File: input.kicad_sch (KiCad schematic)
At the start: 32 parts, among them J15 Screw_Terminal_01x02, J6 Screw_Terminal_01x04, J7 Screw_Terminal_01x04, U2 ADS1113IDGS, U3 TCA9517ADGK, U5 LTV-847S, U6 LTV-847S

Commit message: added part numbers
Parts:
- C1, C2, C3: LCSC (none) -> C49678
- D1, D2, D3, D4, D5, D6, D7, D8: footprint LED_SMD:LED_1206_3216Metric -> LED_SMD:LED_0805_2012Metric_Pad1.15x1.40mm_HandSolder; LCSC (none) -> C2297
- J15: footprint (none) -> Connector_Phoenix_MC:PhoenixContact_MC_1,5_2-G-3.5_1x02_P3.50mm_Horizontal; LCSC (none) -> C61791
- J6, J7: footprint (none) -> Connector_Phoenix_MC:PhoenixContact_MC_1,5_4-G-3.5_1x04_P3.50mm_Horizontal; LCSC (none) -> C5241865
- R1, R2, R3, R4, R5, R6, R7, R8: LCSC (none) -> C17513
- R10, R9: LCSC (none) -> C17477
- U2: LCSC (none) -> C2651336
- U3: LCSC (none) -> C544515
- U5: LCSC (none) -> C114599

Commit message: larger pcb
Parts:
- JP1, JP2: footprint (none) -> Jumper:SolderJumper-2_P1.3mm_Open_Pad1.0x1.5mm
- TP12, TP13: footprint (none) -> TestPoint:TestPoint_Pad_D1.5mm
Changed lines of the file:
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@@
 			)
 		)
-		(property "Footprint" ""
+		(property "Footprint" "Jumper:SolderJumper-2_P1.3mm_Open_Pad1.0x1.5mm"
 			(at 201.93 92.71 0)
 			(effects
@@
 		)
 		(property "Description" "Solder Jumper, 2-pole, open"
+			(at 201.93 92.71 0)
+			(effects
+				(font
+					(size 1.27 1.27)
+				)
+				(hide yes)
+			)
+		)
+		(property "LCSC" ""
 			(at 201.93 92.71 0)
 			(effects
@@
 			)
 		)
-		(property "Footprint" ""
+		(property "Footprint" "TestPoint:TestPoint_Pad_D1.5mm"
 			(at 217.17 59.69 0)
 			(effects
@@
 		)
 		(property "Description" "test point"
+			(at 212.09 59.69 0)
+			(effects
+				(font
+					(size 1.27 1.27)
+				)
+				(hide yes)
+			)
+		)
+		(property "LCSC" ""
 			(at 212.09 59.69 0)
 			(effects
@@
 			)
 		)
-		(property "Footprint" ""
+		(property "Footprint" "TestPoint:TestPoint_Pad_D1.5mm"
 			(at 227.33 59.69 0)
 			(effects
@@
 		)
 		(property "Description" "test point"
+			(at 222.25 59.69 0)
+			(effects
+				(font
+					(size 1.27 1.27)
+				)
+				(hide yes)
+			)
+		)
+		(property "LCSC" ""
 			(at 222.25 59.69 0)
 			(effects
@@
 			)
 		)
-		(property "Footprint" ""
+		(property "Footprint" "Jumper:SolderJumper-2_P1.3mm_Open_Pad1.0x1.5mm"
 			(at 201.93 102.87 0)
 			(effects
@@
 			(at 201.93 102.87 0)
 			(effects
+				(font
+					(size 1.27 1.27)
+				)
+				(hide yes)
+			)
+		)
+		(property "LCSC" ""
+			(at 201.93 102.87 0)
+			(effects

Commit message: added fuse and c for 7805
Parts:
- removed C1, C2: 100nF, Capacitor_SMD:C_0805_2012Metric_Pad1.18x1.45mm_HandSolder, symbol Device:C
- removed U3: TCA9517ADGK, Package_SO:VSSOP-8_3x3mm_P0.65mm, symbol Logic_LevelTranslator:TCA9517ADGK
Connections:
- net SCL: now also JP2.2 (B), TP13.1, U2.10 (SCL)
- net SDA: now also JP1.2 (B), TP12.1, U2.9 (SDA)
- net +5V renamed VCC
- no-connect marks 1 -> 0

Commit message: hat routing finished
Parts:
- R1, R2, R3, R4, R5, R6, R7, R8: footprint Resistor_SMD:R_0805_2012Metric -> Resistor_SMD:R_0805_2012Metric_Pad1.20x1.40mm_HandSolder
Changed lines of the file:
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@@
 			)
 		)
-		(property "Footprint" "Resistor_SMD:R_0805_2012Metric"
+		(property "Footprint" "Resistor_SMD:R_0805_2012Metric_Pad1.20x1.40mm_HandSolder"
 			(at 72.39 32.258 90)
 			(effects
@@
 			)
 		)
-		(property "Footprint" "Resistor_SMD:R_0805_2012Metric"
+		(property "Footprint" "Resistor_SMD:R_0805_2012Metric_Pad1.20x1.40mm_HandSolder"
 			(at 72.39 74.168 90)
 			(effects
@@
 			)
 		)
-		(property "Footprint" "Resistor_SMD:R_0805_2012Metric"
+		(property "Footprint" "Resistor_SMD:R_0805_2012Metric_Pad1.20x1.40mm_HandSolder"
 			(at 72.39 112.268 90)
 			(effects
@@
 			)
 		)
-		(property "Footprint" "Resistor_SMD:R_0805_2012Metric"
+		(property "Footprint" "Resistor_SMD:R_0805_2012Metric_Pad1.20x1.40mm_HandSolder"
 			(at 72.39 126.238 90)
 			(effects
@@
 			)
 		)
-		(property "Footprint" "Resistor_SMD:R_0805_2012Metric"
+		(property "Footprint" "Resistor_SMD:R_0805_2012Metric_Pad1.20x1.40mm_HandSolder"
 			(at 72.39 140.208 90)
 			(effects
@@
 			)
 		)
-		(property "Footprint" "Resistor_SMD:R_0805_2012Metric"
+		(property "Footprint" "Resistor_SMD:R_0805_2012Metric_Pad1.20x1.40mm_HandSolder"
 			(at 72.39 46.228 90)
 			(effects
@@
 			)
 		)
-		(property "Footprint" "Resistor_SMD:R_0805_2012Metric"
+		(property "Footprint" "Resistor_SMD:R_0805_2012Metric_Pad1.20x1.40mm_HandSolder"
 			(at 72.39 60.198 90)
 			(effects
@@
 			)
 		)
-		(property "Footprint" "Resistor_SMD:R_0805_2012Metric"
+		(property "Footprint" "Resistor_SMD:R_0805_2012Metric_Pad1.20x1.40mm_HandSolder"
 			(at 72.39 98.298 90)
 			(effects

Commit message: von ben
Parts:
- removed TP12: SDA, TestPoint:TestPoint_Pad_D1.5mm, symbol Connector:TestPoint
- removed TP13: SCL, TestPoint:TestPoint_Pad_D1.5mm, symbol Connector:TestPoint
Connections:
- net at R9.2, U2.4 (AIN0): no longer JP1.1 (A)
- net at J15.2 (Pin_2), R10.1: now also JP2.1 (A)
- net at R10.2, U2.5 (AIN1): no longer JP2.1 (A)
- net at J15.1 (Pin_1), R9.1: now also JP1.1 (A)
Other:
- moved on the sheet: R10, R9

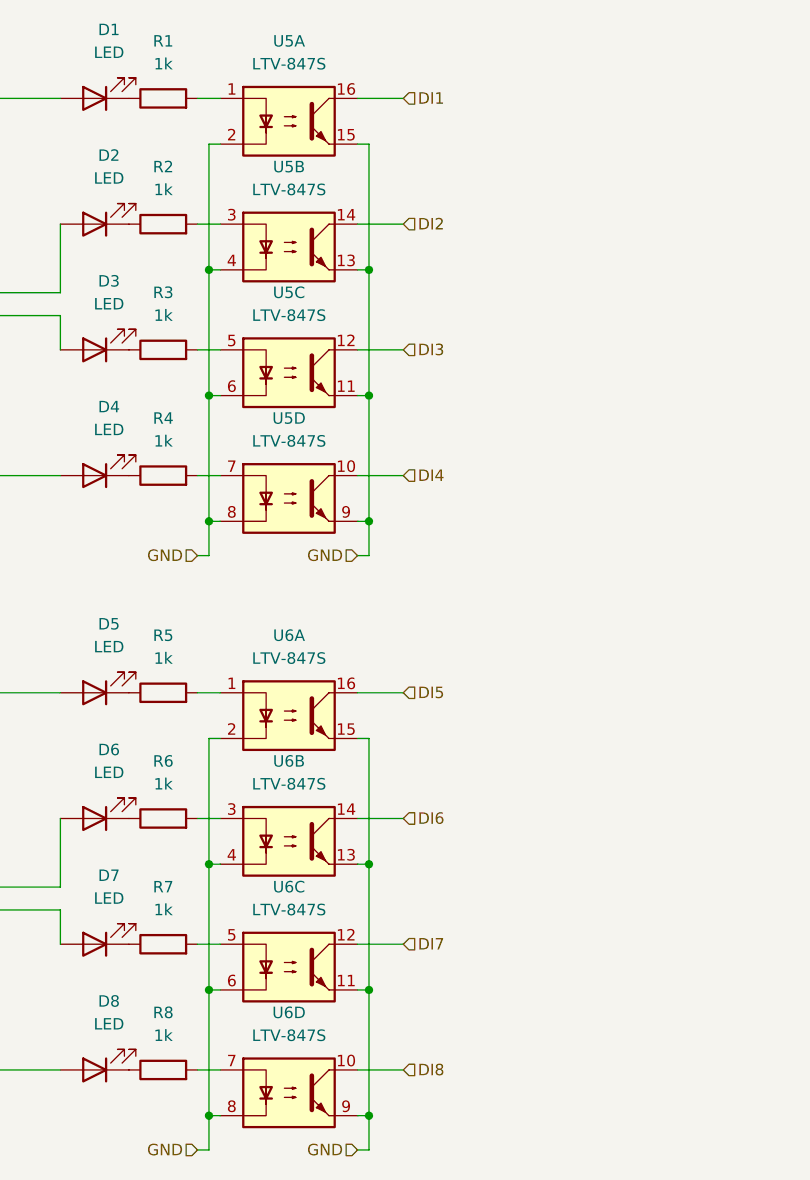
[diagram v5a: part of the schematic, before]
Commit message: pcb layout finished
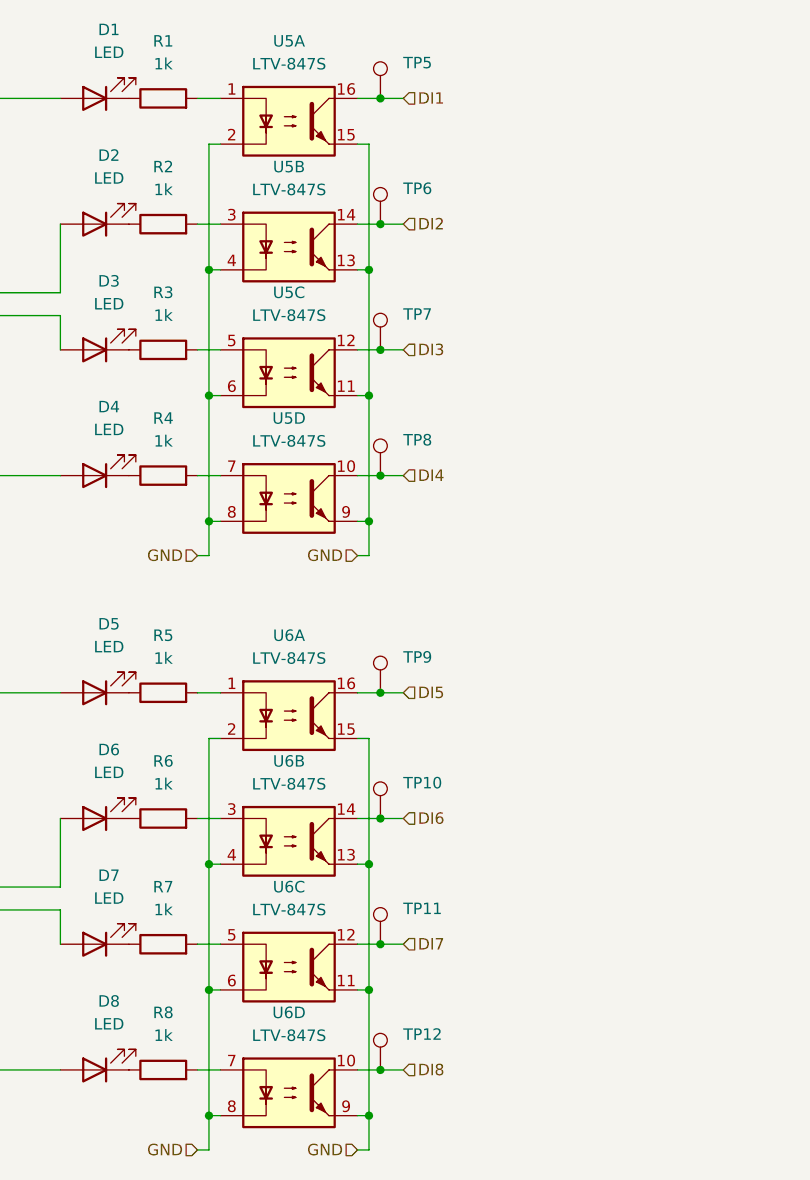
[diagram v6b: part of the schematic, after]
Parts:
- added TP10, TP11, TP12, TP5, TP6, TP7, TP8, TP9: ~, TestPoint:TestPoint_Pad_D1.5mm, symbol Connector:TestPoint
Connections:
- net DI1: now also TP5.1
- net DI2: now also TP6.1
- net DI3: now also TP7.1
- net DI4: now also TP8.1
- net DI5: now also TP9.1
- net DI6: now also TP10.1
- net DI7: now also TP11.1
- net DI8: now also TP12.1
